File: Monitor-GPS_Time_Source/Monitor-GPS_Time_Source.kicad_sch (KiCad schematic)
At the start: 17 parts, among them J1 Conn 2x5, 1.27mm, J2 Conn 1x10, 2.54mm, J3 Conn 1x10, 2.54mm, J4 Conn 1x3, 2.54mm, SW2 SW_Push, U1 MSPM0L110x, U2 BL8565

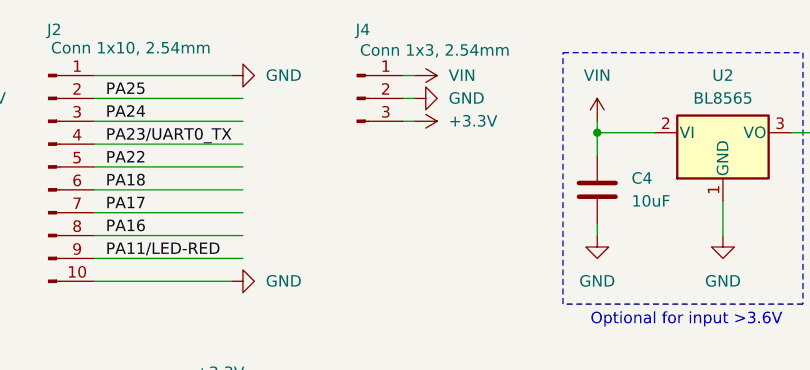
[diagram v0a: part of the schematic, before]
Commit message: Updated silkscreen for MSPM0. Finished DRC edits
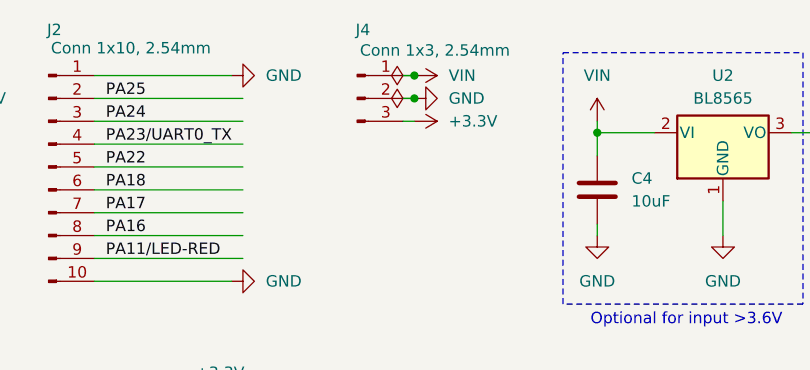
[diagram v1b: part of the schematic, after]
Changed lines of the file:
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@@
 	(paper "A4")
 	(junction
+		(at 163.83 30.48)
+		(diameter 0)
+		(color 0 0 0 0)
+	)
+	(junction
 		(at 91.44 99.06)
 		(diameter 0)
@@
 	)
 	(junction
+		(at 163.83 33.02)
+		(diameter 0)
+		(color 0 0 0 0)
+	)
+	(junction
 		(at 210.82 36.83)
 		(diameter 0)
@@
 	)
 	(symbol
+		(lib_id "power:PWR_FLAG")
+		(at 163.83 33.02 90)
+		(unit 1)
+		(exclude_from_sim no)
+		(in_bom yes)
+		(on_board yes)
+		(dnp no)
+		(fields_autoplaced yes)
+		(property "Reference" "#FLG02"
+			(at 161.925 33.02 0)
+			(effects
+				(font
+					(size 1.27 1.27)
+				)
+				(hide yes)
+			)
+		)
+		(property "Value" "PWR_FLAG"
+			(at 160.02 33.0199 90)
+			(effects
+				(font
+					(size 1.27 1.27)
+				)
+				(justify left)
+				(hide yes)
+			)
+		)
+		(property "Footprint" ""
+			(at 163.83 33.02 0)
+			(effects
+				(font
+					(size 1.27 1.27)
+				)
+				(hide yes)
+			)
+		)
+		(property "Datasheet" "~"
+			(at 163.83 33.02 0)
+			(effects
+				(font
+					(size 1.27 1.27)
+				)
+				(hide yes)
+			)
+		)
+		(property "Description" "Special symbol for telling ERC where power comes from"
+			(at 163.83 33.02 0)
+			(effects
+				(font
+					(size 1.27 1.27)
+				)
+				(hide yes)
+			)
+		)
+		(pin "1"
+		)
+		(instances
+			(project "Monitor-GPS_Time_Source"
+				(path "/e8ca792e-d887-4acf-b1e0-80c90e1318df"
+					(reference "#FLG02")
+					(unit 1)
+				)
+			)
+		)
+	)
+	(symbol
 		(lib_id "Device:LED_Dual_AKA")
 		(at 128.27 154.94 0)
@@
 					(unit 1)
 				)
+			)
+		)
+	)
+	(symbol
+		(lib_id "power:PWR_FLAG")
+		(at 163.83 30.48 90)
+		(unit 1)
+		(exclude_from_sim no)
+		(in_bom yes)
+		(on_board yes)
+		(dnp no)
+		(fields_autoplaced yes)
+		(property "Reference" "#FLG01"
+			(at 161.925 30.48 0)
+			(effects
+				(font
+					(size 1.27 1.27)
+				)
+				(hide yes)
+			)
+		)
+		(property "Value" "PWR_FLAG"
+			(at 160.02 30.4799 90)
+			(effects
+				(font
+					(size 1.27 1.27)
+				)
+				(justify left)
+				(hide yes)
+			)
+		)
+		(property "Footprint" ""
+			(at 163.83 30.48 0)
+			(effects
+				(font
+					(size 1.27 1.27)
+				)
+				(hide yes)
+			)
+		)
+		(property "Datasheet" "~"
+			(at 163.83 30.48 0)
+			(effects
+				(font
+					(size 1.27 1.27)
+				)
+				(hide yes)
+			)
+		)
+		(property "Description" "Special symbol for telling ERC where power comes from"
+			(at 163.83 30.48 0)
+			(effects
+				(font
+					(size 1.27 1.27)
+				)
+				(hide yes)
+			)
+		)
+		(pin "1"
+		)
+		(instances
+			(project ""
+				(path "/e8ca792e-d887-4acf-b1e0-80c90e1318df"
+					(reference "#FLG01")
+					(unit 1)
+				)
